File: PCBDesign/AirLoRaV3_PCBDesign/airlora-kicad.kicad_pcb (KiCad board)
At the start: 4 copper layers, 60 x 60 mm, 89 parts, among them IC1 BALFHB-WL-05D3, J1 12V, J2 Conn_Coaxial, J3 DHT, J4 UART1, J5 UART2, J6 I2C, J7 UART2, Q1 S8050, Q2 S8050, Q3 S8050, Q4 S8050, SW1 SW_Push, U1 TPS54202DDC, U2 TPS7A2633DRVR, U3 BGS12WN6E6327, U4 STM32WLE5JCIx, Y1 NX2012SA 32.768KHz

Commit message: Update circuit buck converter and sensor
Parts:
- removed the C17 at (162.3, 88.8)
- removed the C23 at (162.3, 90.3)
- removed the C29 at (158.0, 81.7)
- removed the C31 at (150.1, 96.7)
- removed the C33 at (150.1, 98.2)
- removed the C35 at (151.9, 81.7)
- removed the C36 at (162.3, 87.3)
- removed L5: 1400R 1GHz, Inductor_SMD:L_0603_1608Metric
- removed XTAL1: NT2016SA-32M-END4263A, footprint:NT2016SA-32M-END4263A_NDK
- added C18: 0.47uF, Capacitor_SMD:C_0603_1608Metric, F.Cu at (68.8, 133.7)
- added C27: 4.7uF, Capacitor_SMD:C_0603_1608Metric, F.Cu at (68.8, 136.8)
- added C28: 100nF, Capacitor_SMD:C_0603_1608Metric, F.Cu at (68.8, 135.2)
- added C37: 4.7uf, Capacitor_SMD:C_0805_2012Metric, F.Cu at (228.3, 85.6)
- added C38: 100nf, Capacitor_SMD:C_0603_1608Metric, F.Cu at (234.3, 83.8)
- added C40: 100nf, Capacitor_SMD:C_0603_1608Metric, F.Cu at (245.9, 88.8)
- added C41: 100nf, Capacitor_SMD:C_0603_1608Metric, F.Cu at (239.8, 99.6)
- added C42: 100nf, Capacitor_SMD:C_0603_1608Metric, F.Cu at (228.1, 92.6)
- added C43: 22PF, Capacitor_SMD:C_0603_1608Metric, F.Cu at (225.4, 99.6)
- added C44: 22PF, Capacitor_SMD:C_0603_1608Metric, F.Cu at (214.8, 86.0)
- added C45: 100nF, Capacitor_SMD:C_0603_1608Metric, F.Cu at (214.8, 88.5)
- added C46: 1uF, Capacitor_SMD:C_0805_2012Metric_Pad1.18x1.45mm_HandSolder, F.Cu at (84.5, 69.5)
- added C47: 1uF, Capacitor_SMD:C_0805_2012Metric_Pad1.18x1.45mm_HandSolder, F.Cu at (84.3, 64.0)
- added D4: LED, LED_SMD:LED_0603_1608Metric_Pad1.05x0.95mm_HandSolder, F.Cu at (220.4, 90.6)
- added D5: LED, LED_SMD:LED_0603_1608Metric_Pad1.05x0.95mm_HandSolder, F.Cu at (68.5, 79.4)
- added J3: LED, Connector_JST:JST_XA_B02B-XASK-1-A_1x02_P2.50mm_Vertical, F.Cu at (50.3, 122.6)
- added Q1: S8050, Package_TO_SOT_SMD:SOT-23, F.Cu at (42.7, 124.4)
- added Q6: ZVP2106GTA, Package_TO_SOT_SMD:SOT-223-3_TabPin2, F.Cu at (89.4, 96.6)
- added R13: 1K, Resistor_SMD:R_0603_1608Metric, F.Cu at (39.1, 123.5)
- added R19: 1k, Resistor_SMD:R_0603_1608Metric, F.Cu at (214.8, 91.1)
- added R20: 10k, Resistor_SMD:R_0603_1608Metric, F.Cu at (214.8, 93.6)
- added R21: 10k, Resistor_SMD:R_0603_1608Metric, F.Cu at (214.8, 96.1)
- added R22: 10K, Resistor_SMD:R_0603_1608Metric, F.Cu at (77.0, 66.4)
- added R23: 1.96M, Resistor_SMD:R_0603_1608Metric, F.Cu at (80.0, 66.4)
- added R24: 1.18M, Resistor_SMD:R_0603_1608Metric, F.Cu at (80.1, 68.1)
- added R25: 1k, Resistor_SMD:R_0603_1608Metric, F.Cu at (68.5, 81.0)
- added R26: 10K, Resistor_SMD:R_0603_1608Metric, F.Cu at (82.5, 99.1)
- added R27: 1K, Resistor_SMD:R_0603_1608Metric, F.Cu at (204.3, 106.3)
- added SW2: SW_Slide_DPDT, Button_Switch_THT:SW_E-Switch_EG1271_SPDT, F.Cu at (104.5, 67.9)
- added SW3: SW_Push, Button_Switch_SMD:SW_Push_SPST_NO_Alps_SKRK, F.Cu at (232.7, 104.5)
- added U5: STM32F103C8Tx, Package_QFP:LQFP-48_7x7mm_P0.5mm, F.Cu at (237.1, 91.5)
- added U6: TPS7A2633DRVR, footprint:TPS7A2633DRVR, F.Cu at (84.3, 66.7)
- added X1: NX2016SA-32MHZ, footprint:NX2016SA_NDK, F.Cu at (86.8, 142.5)
- added Y2: 8Mhz, Crystal:Crystal_SMD_3225-4Pin_3.2x2.5mm, F.Cu at (226.0, 103.1)
- C16: renamed from C32; value 5.1pF -> 6.8pF
- C22: renamed from C34; value 10pF -> 6.8pF
- C39: value 100nF -> 100nf
- D1: value 1N4007 -> D_Zener; footprint Diode_SMD:D_SMA -> Diode_SMD:D_SMA_Handsoldering
- IC1: value BALFHB-WL-05D3 -> BALFHB-WL-02D3
- R12: value 220 -> 10K
- U4: value STM32WLE5JCIx -> STM32WLE5CCUx; footprint Package_BGA:ST_UFBGA-73_5x5mm_Layout9x9_P0.5mm -> Package_DFN_QFN:QFN-48-1EP_7x7mm_P0.5mm_EP5.6x5.6mm
- moved H1 225.8 mm to (-46.3, 111.3)
- moved H2 225.8 mm to (-46.3, 61.3)
- moved H3 225.8 mm to (-96.3, 111.3)
- moved H4 225.8 mm to (-96.3, 61.3)
- moved C11 104.8 mm to (269.2, 128.8)
- moved C12 104.8 mm to (266.5, 131.2)
- moved C14 104.8 mm to (266.5, 132.8)
- moved C17 104.8 mm to (262.0, 125.8)
- moved L2 104.8 mm to (274.5, 128.8)
- moved C10 104.8 mm to (271.8, 129.6)
- moved C13 104.8 mm to (267.6, 124.3)
- moved C15 104.8 mm to (267.6, 125.8)
- moved C9 104.8 mm to (277.1, 129.6)
- moved IC1 104.8 mm to (263.0, 128.8)
- moved J2 104.8 mm to (280.7, 128.9)
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- renumbered C21 to C17, C16 to C19, C18 to C20, C19 to C21, C22 to C23, C26 to C24, C28 to C25, C30 to C26, C20 to C29, C24 to C30, C25 to C31, C27 to C32, C37 to C33, C38 to C34, C40 to C35, C41 to C36, J3 to J4, J4 to J5, J5 to J6, J6 to J7, J7 to J8, Q1 to Q2, Q2 to Q3, Q3 to Q4, Q4 to Q5, R13 to R14, R14 to R15, R15 to R16, R16 to R17, R17 to R18
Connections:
- C12 pad 1: Net-(U3-VDD) -> GND
- C12 pad 2: GND -> Net-(U3-VDD)
- C14 pad 1: Net-(U3-VDD) -> GND
- C14 pad 2: GND -> Net-(U3-VDD)
- C16 pad 2: Net-(XTAL1-VCC) -> Net-(U4-OSC_IN)
- C21 pad 1: VDDPA -> VDDRF1V55
- C22 pad 1: Net-(C34-Pad1) -> Net-(U4-OSC_OUT)
- C22 pad 2: XTA -> GND
- C24 pad 1: VDDRF -> +3.3V
- C25 pad 1: VREF+ -> Net-(U4-VDDA)
- C26 pad 1: VREF+ -> Net-(U4-VDDA)
- C29 pad 1: VDDRF -> +3.3V
- C30 pad 1: VDDRF -> +3.3V
- C31 pad 1: VDDRF -> +3.3V
- C32 pad 1: VDDRF -> +3.3V
- C35 pad 1: VDDPA -> VDDRF1V55
- C39 pad 1: VDDPA -> 3.3V
- C8 pad 1: VDDRF -> +3.3V
- D3 pad 2: VDDRF -> +3.3V
- J1 pad 1: Net-(D1-A) -> Net-(J1-Pin_1)
- J4 pad 2: /AirLora V3/MCU/PA11 -> /AirLora V3/MCU Sub/PA1
- J5 pad 3: /AirLora V3/MCU/PA9_TX -> /AirLora V3/MCU Sub/TX3
- J5 pad 4: /AirLora V3/MCU/PA10_RX -> /AirLora V3/MCU Sub/RX3
- J6 pad 3: /AirLora V3/MCU/PA3_RX -> /AirLora V3/MCU Sub/RX2
- J6 pad 4: /AirLora V3/MCU/PA2_TX -> /AirLora V3/MCU Sub/TX2
- J7 pad 3: /AirLora V3/MCU/PB8_SCL -> /AirLora V3/MCU Sub/SDA1
- J7 pad 4: /AirLora V3/MCU/PB9_SDA -> /AirLora V3/MCU Sub/SCL1
- J8 pad 2: VDDRF -> +3.3V
- J8 pad 3: /AirLora V3/MCU/T_SWCLK -> Net-(J8-Pin_3)
- J8 pad 4: /AirLora V3/MCU/T_SWDIO -> Net-(J8-Pin_4)
- L3 pad 1: VDDPA -> VDDRF1V55
- L4 pad 1: VDDRF -> +3.3V
- L4 pad 2: VREF+ -> Net-(U4-VDDA)
- R1 pad 2: /AirLora V3/MCU/PA12 -> /AirLora V3/MCU/PB3
- R10 pad 1: VDDRF -> +3.3V
- R12 pad 1: Net-(XTAL1-OUTPUT) -> GND
- R12 pad 2: Net-(C34-Pad1) -> Net-(U4-PH3)
- R14 pad 1: /AirLora V3/MCU/PA11 -> /AirLora V3/MCU Sub/PA1
- R15 pad 2: /AirLora V3/MCU/PB2 -> /AirLora V3/MCU Sub/PA7
- R16 pad 1: /AirLora V3/MCU/PA6 -> /AirLora V3/MCU Sub/PA6
- R17 pad 1: /AirLora V3/MCU/PA5 -> /AirLora V3/MCU Sub/PA5
- R18 pad 1: /AirLora V3/MCU/PA8 -> /AirLora V3/MCU Sub/PA4
- R6 pad 2: VDDRF -> +3.3V
- R7 pad 1: VDDRF -> +3.3V
- U2 pad 1: VDDRF -> +3.3V
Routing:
- net +5V: track 140.1 -> 24.1 mm, vias 4 -> 0
- net VDDRF: track 79.7 -> 15.0 mm, vias 13 -> 0
- net /AirLora V3/MCU/PA12: track 42.7 -> 0.00 mm, vias 2 -> 0
- net /AirLora V3/MCU/PB9_SDA: track 37.8 -> 0.00 mm, vias 1 -> 0
- net 12V: track 37.1 -> 0.00 mm
- net /AirLora V3/MCU/PA11: track 33.6 -> 0.00 mm, vias 1 -> 0
- net +3.3V: track 0.00 -> 33.1 mm, vias 0 -> 5
- net /AirLora V3/MCU/PA9_TX: track 32.7 -> 0.00 mm, vias 1 -> 0
- net /AirLora V3/MCU/PB8_SCL: track 31.4 -> 0.00 mm, vias 1 -> 0
- net /AirLora V3/MCU/T_SWDIO: track 27.4 -> 0.00 mm, vias 1 -> 0
- net /AirLora V3/MCU/T_SWCLK: track 27.2 -> 1.76 mm
- net /AirLora V3/MCU/PA5: track 25.1 -> 0.00 mm, vias 2 -> 0
- net /AirLora V3/MCU/PB2: track 24.7 -> 0.00 mm, vias 3 -> 0
- net /AirLora V3/MCU/PA10_RX: track 24.2 -> 0.00 mm, vias 1 -> 0
- net /AirLora V3/MCU/PA2_TX: track 23.2 -> 0.00 mm, vias 1 -> 0
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- removed copper zone on In2.Cu, net VDDPA

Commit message: Update schematic
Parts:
- added J10: A_NO2, Connector_JST:JST_XH_B3B-XH-A_1x03_P2.50mm_Vertical, F.Cu at (197.5, 73.2)
- added J11: A_CO, Connector_JST:JST_XH_B3B-XH-A_1x03_P2.50mm_Vertical, F.Cu at (197.1, 85.0)
- added J6: I2C, Connector_Molex:Molex_CLIK-Mate_502585-0470_1x04-1MP_P1.50mm_Horizontal, F.Cu at (167.5, 42.1)
- added Q10: S8050, Package_TO_SOT_SMD:SOT-23, F.Cu at (191.0, 87.2)
- added Q3: S8050, Package_TO_SOT_SMD:SOT-23, F.Cu at (170.5, 107.8)
- added Q6: S8050, Package_TO_SOT_SMD:SOT-23, F.Cu at (170.2, 48.9)
- added Q9: S8050, Package_TO_SOT_SMD:SOT-23, F.Cu at (191.3, 77.3)
- added R20: 1K, Resistor_SMD:R_0603_1608Metric, F.Cu at (171.4, 104.0)
- added R24: 1K, Resistor_SMD:R_0603_1608Metric, F.Cu at (170.3, 53.0)
- added R30: 1K, Resistor_SMD:R_0603_1608Metric, F.Cu at (187.3, 77.3)
- added R31: 1K, Resistor_SMD:R_0603_1608Metric, F.Cu at (186.9, 87.3)
- J3: value LED -> Led; footprint Connector_JST:JST_XA_B02B-XASK-1-A_1x02_P2.50mm_Vertical -> Connector_JST:JST_XH_B3B-XH-A_1x03_P2.50mm_Vertical
- J4: footprint Connector_JST:JST_XH_B3B-XH-A_1x03_P2.50mm_Vertical -> Connector_Molex:Molex_CLIK-Mate_502585-0370_1x03-1MP_P1.50mm_Horizontal
- J5: footprint Connector_JST:JST_XH_B4B-XH-A_1x04_P2.50mm_Vertical -> Connector_Molex:Molex_CLIK-Mate_502585-0470_1x04-1MP_P1.50mm_Horizontal
- J7: renamed from J6; footprint Connector_JST:JST_XH_B4B-XH-A_1x04_P2.50mm_Vertical -> Connector_Molex:Molex_CLIK-Mate_502585-0470_1x04-1MP_P1.50mm_Horizontal
- J8: renamed from J7; footprint Connector_JST:JST_XH_B4B-XH-A_1x04_P2.50mm_Vertical -> Connector_Molex:Molex_CLIK-Mate_502585-0470_1x04-1MP_P1.50mm_Horizontal
- moved H2 248.8 mm to (201.5, 38.8)
- moved H1 247.8 mm to (201.5, 113.7)
- moved H4 229.8 mm to (132.4, 38.8)
- moved H3 228.7 mm to (132.4, 113.7)
- moved Q8 143.0 mm to (145.2, 48.7), turned to 90 degrees
- moved R26 137.9 mm to (145.3, 51.6), turned to 180 degrees
- moved R19 128.7 mm to (166.2, 103.9), turned to -90 degrees
- moved Q2 123.7 mm to (165.3, 107.8), turned to -90 degrees
- moved J3 119.6 mm to (169.6, 114.0), turned to 180 degrees
- moved U5 103.0 mm to (168.8, 90.2)
- moved C21 103.0 mm to (174.0, 81.3)
- moved C24 103.0 mm to (180.6, 95.1)
- moved C32 103.0 mm to (177.2, 82.9)
- moved C34 103.0 mm to (160.4, 91.1)
- moved C18 103.0 mm to (175.8, 95.3)
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- renumbered C8 to C10, C9 to C11, C10 to C12, C11 to C13, C12 to C14, C13 to C15, C14 to C16, C15 to C17, C16 to C18, C17 to C19, C46 to C2, C18 to C20, C19 to C21, C20 to C22, C21 to C23, C22 to C24, C23 to C25, C24 to C26, C25 to C27, C26 to C28, C27 to C29, C2 to C3, C28 to C30, C29 to C31, C30 to C32, C31 to C33, C32 to C34, C33 to C35, C34 to C36, C35 to C37, C36 to C38, C37 to C39, C3 to C4, C38 to C40, C39 to C41, C40 to C42, C41 to C43, C42 to C44, C43 to C45, C44 to C46, C45 to C47, C4 to C5, C5 to C6, C47 to C7, C6 to C8, C7 to C9, D5 to D3, D3 to D4, D4 to D5, J8 to J9, Q6 to Q1, Q1 to Q2, Q2 to Q4, Q3 to Q5, Q4 to Q7, Q5 to Q8, R26 to R1, R25 to R10, R6 to R11, R7 to R12, R8 to R13, R9 to R14, R10 to R15, R11 to R16, R12 to R17, R27 to R18, R13 to R19, R1 to R2, R14 to R21, R15 to R22, R16 to R23, R17 to R25, R18 to R26, R19 to R27, R20 to R28, R21 to R29, R2 to R3, R3 to R4, R22 to R5, R4 to R6, R23 to R7, R24 to R8, R5 to R9, U6 to U2, U2 to U3, U3 to U4, U4 to U5, U5 to U6
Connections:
- J3 pad 2: +5V -> Net-(J3-Pin_2)
- J5 pad 3: /AirLora V3/MCU Sub/TX3 -> /AirLora V3/MCU Sub/RX3
- J5 pad 4: /AirLora V3/MCU Sub/RX3 -> /AirLora V3/MCU Sub/TX3
- J7 pad 3: /AirLora V3/MCU Sub/RX2 -> /AirLora V3/MCU Sub/SCL1
- J7 pad 4: /AirLora V3/MCU Sub/TX2 -> /AirLora V3/MCU Sub/SDA1
- J8 pad 3: /AirLora V3/MCU Sub/SDA1 -> /AirLora V3/MCU Sub/SCL1
- J8 pad 4: /AirLora V3/MCU Sub/SCL1 -> /AirLora V3/MCU Sub/SDA1
- Q2 pad 2: Net-(J3-Pin_1) -> +5V
- Q2 pad 3: GND -> Net-(J3-Pin_2)
- R23 pad 1: /AirLora V3/MCU Sub/PA6 -> /AirLora V3/MCU Sub/PA5
- R25 pad 1: /AirLora V3/MCU Sub/PA5 -> /AirLora V3/MCU Sub/PA4
- R26 pad 1: /AirLora V3/MCU Sub/PA4 -> /AirLora V3/MCU Sub/PA6
- U5 pad 9: unconnected-(U4-PA2-Pad9) -> Net-(U5-PA2)
- U6 pad 18: unconnected-(U5-PB0-Pad18) -> /AirLora V3/MCU Sub/PB0
- U6 pad 19: unconnected-(U5-PB1-Pad19) -> /AirLora V3/MCU Sub/PB1
- U6 pad 38: unconnected-(U5-PA15-Pad38) -> /AirLora V3/MCU Sub/PA15
- U6 pad 39: unconnected-(U5-PB3-Pad39) -> /AirLora V3/MCU Sub/PB3
- U6 pad 40: unconnected-(U5-PB4-Pad40) -> /AirLora V3/MCU Sub/PB4
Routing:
- net Net-(J4-Pin_3): track 16.8 -> 0.00 mm
- net +3.3V: track 33.1 -> 19.3 mm, vias 5 -> 0
- net /AirLora V3/MCU Sub/PA1: track 8.47 -> 0.00 mm
- net Net-(U3-NC): track 6.22 -> 0.00 mm
- net +5V: track 24.1 -> 18.2 mm
- net GND: track 0.27 -> 5.94 mm
- net Net-(U4-VDD): track 5.67 -> 0.00 mm
- net Net-(J7-Pin_2): track 5.11 -> 0.00 mm
- net /AirLora V3/MCU Sub/TX2: track 4.27 -> 0.00 mm
- net Net-(U3-PG): track 2.12 -> 0.00 mm
- net Net-(Q7-B): track 1.69 -> 0.00 mm
- net Net-(Q8-B): track 1.62 -> 0.00 mm
- net /AirLora V3/MCU Sub/RX2: track 1.29 -> 0.00 mm
- net /AirLora V3/MCU Sub/PA4: track 0.95 -> 0.00 mm
- removed copper zone on F.Cu, net VDDRF
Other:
- board size 60 x 60 mm -> 79.1 x 84.9 mm

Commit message: Update PCB
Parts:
- removed the C38 at (192.9, 48.9)
- removed the R21 at (192.9, 50.4)
- J4: value DHT -> SHT; footprint Connector_Molex:Molex_CLIK-Mate_502585-0370_1x03-1MP_P1.50mm_Horizontal -> Connector_JST:JST_XH_B4B-XH-A_1x04_P2.50mm_Vertical
- J9: renamed from J7; value UART2 -> I2C
- SW3: footprint Button_Switch_SMD:SW_Push_SPST_NO_Alps_SKRK -> Button_Switch_SMD:SW_Push_1P1T_NO_Vertical_Wuerth_434133025816
- moved SW1 36.0 mm to (160.5, 94.1)
- moved Q7 33.5 mm to (149.1, 50.8)
- moved J7 33.5 mm to (146.8, 43.7)
- moved R24 33.5 mm to (149.2, 53.7)
- moved C22 32.7 mm to (156.6, 94.0), turned to -90 degrees
- moved R29 24.7 mm to (161.3, 75.9), turned to -90 degrees
- moved SW3 22.6 mm to (157.5, 75.6)
- moved C46 21.1 mm to (153.7, 75.9), turned to 90 degrees
- moved R26 17.5 mm to (175.1, 53.1), turned to 0 degrees
- moved J10 17.4 mm to (159.5, 43.7)
- moved J5 17.4 mm to (184.9, 43.7)
- moved J9 17.4 mm to (172.2, 43.7)
- moved Q10 17.4 mm to (162.5, 50.3)
- moved Q4 17.4 mm to (187.5, 50.5)
- moved Q9 17.4 mm to (175.0, 50.3)
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- renumbered C2 to C1, C1 to C2, C39 to C38, C40 to C39, C41 to C40, C42 to C41, C43 to C42, C44 to C43, C45 to C44, C46 to C45, C47 to C46, C7 to C6, C6 to C7, D3 to D2, D2 to D3, J8 to J10, J9 to J11, J6 to J5, J10 to J6, J5 to J7, J11 to J8, Q8 to Q10, Q6 to Q4, Q4 to Q5, Q9 to Q6, Q5 to Q7, Q10 to Q8, Q7 to Q9, R9 to R10, R24 to R21, R30 to R23, R23 to R24, R31 to R25, R25 to R26, R26 to R27, R27 to R28, R28 to R29, R5 to R3, R29 to R30, R7 to R4, R8 to R5, R3 to R6, R4 to R7, R6 to R8, R10 to R9, U2 to U1, U1 to U2
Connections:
- net 12V renamed +12V
- net 3.3V renamed +3.3V_HP
- J4 pad 2: /AirLora V3/MCU Sub/PA1 -> Net-(J4-Pin_2)
- J4 pad 3: Net-(J4-Pin_3) -> /AirLora V3/MCU Sub/SCL1
- Q5 pad 3: Net-(J4-Pin_3) -> Net-(J4-Pin_2)
- R19 pad 1: Net-(U5-PA1) -> Net-(U5-PA5)
- R2 pad 2: /AirLora V3/MCU/PB3 -> /AirLora V3/MCU/PA3
- R20 pad 1: Net-(U5-PA2) -> Net-(U5-PA6)
- R23 pad 1: /AirLora V3/MCU Sub/PB4 -> /AirLora V3/MCU Sub/PA6
- R25 pad 1: /AirLora V3/MCU Sub/PB3 -> /AirLora V3/MCU Sub/PA4
- R26 pad 1: /AirLora V3/MCU Sub/PA4 -> /AirLora V3/MCU Sub/PB3
- R27 pad 1: /AirLora V3/MCU Sub/PA6 -> /AirLora V3/MCU Sub/PB4
- U5 pad 1: /AirLora V3/MCU/PB3 -> unconnected-(U5-PB3-Pad1)
- U5 pad 10: unconnected-(U5-PA3-Pad10) -> /AirLora V3/MCU/PA3
- U5 pad 13: unconnected-(U5-PA5-Pad13) -> Net-(U5-PA5)
- U5 pad 14: unconnected-(U5-PA6-Pad14) -> Net-(U5-PA6)
- U5 pad 34: unconnected-(U5-PA11-Pad34) -> /AirLora V3/MCU Sub/SCL2
- U5 pad 35: unconnected-(U5-PA12-Pad35) -> /AirLora V3/MCU Sub/SDA2
- U5 pad 4: /AirLora V3/MCU Sub/SCL2 -> unconnected-(U5-PB6-Pad4)
- U5 pad 5: /AirLora V3/MCU Sub/SDA2 -> unconnected-(U5-PB7-Pad5)
- U5 pad 8: Net-(U5-PA1) -> unconnected-(U5-PA1-Pad8)
- U5 pad 9: Net-(U5-PA2) -> unconnected-(U5-PA2-Pad9)
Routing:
- net +5V: track 18.2 -> 260.8 mm, vias 0 -> 8
- net +3.3V: track 19.3 -> 160.9 mm, vias 0 -> 8
- net +3.3V_HP: track 0.00 -> 112.8 mm, vias 0 -> 3
- net /AirLora V3/MCU Sub/SDA1: track 0.00 -> 79.1 mm, vias 0 -> 2
- net /AirLora V3/MCU Sub/SCL1: track 0.00 -> 64.7 mm, vias 0 -> 2
- net +12V: track 0.00 -> 48.9 mm, vias 0 -> 2
- net /AirLora V3/MCU Sub/TX3: track 0.00 -> 41.3 mm, vias 0 -> 2
- net /AirLora V3/MCU Sub/RX3: track 0.00 -> 41.3 mm, vias 0 -> 2
- net /AirLora V3/MCU Sub/PB1: track 0.00 -> 41.2 mm
- net /AirLora V3/MCU Sub/PA7: track 0.00 -> 37.3 mm, vias 0 -> 2
- net /AirLora V3/MCU Sub/SDA2: track 0.00 -> 36.4 mm, vias 0 -> 2
- net /AirLora V3/MCU Sub/SCL2: track 0.00 -> 34.0 mm, vias 0 -> 2
- net /AirLora V3/MCU Sub/PA4: track 0.00 -> 32.2 mm, vias 0 -> 2
- net /AirLora V3/MCU Sub/PB0: track 0.00 -> 32.2 mm, vias 0 -> 1
- net /AirLora V3/MCU Sub/PA8: track 0.00 -> 31.4 mm, vias 0 -> 2
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- added copper zone on F.Cu, net +3.3V
- added copper zone on F.Cu, net +3.3V_HP
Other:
- board size 79.1 x 84.9 mm -> 77 x 77 mm

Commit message: Update PCB
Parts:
- moved R2 0.41 mm to (138.6, 86.4)
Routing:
- net /AirLora V3/MCU Sub/PA8: track 31.4 -> 35.7 mm
- net Net-(J4-Pin_2): track 17.8 -> 14.3 mm
- net /AirLora V3/MCU Sub/PB1: track 41.2 -> 43.7 mm
- net Net-(U5-PA5): track 11.4 -> 12.8 mm
- net Net-(U5-PC13): track 25.9 -> 25.1 mm
- net /AirLora V3/MCU Sub/SDA1: track 79.1 -> 79.9 mm
- net /AirLora V3/MCU/T_SWCLK: track 25.0 -> 24.3 mm
- net Net-(U5-NRST): track 15.7 -> 16.4 mm
- net +5V: track 260.8 -> 261.3 mm
- net +3.3V_HP: track 112.8 -> 113.3 mm

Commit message: Update package and placement components
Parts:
- added C47: 0.47uF, Capacitor_SMD:C_0402_1005Metric_Pad0.74x0.62mm_HandSolder, F.Cu at (185.4, 91.5)
- added C48: 470nF, Capacitor_SMD:C_0402_1005Metric_Pad0.74x0.62mm_HandSolder, F.Cu at (185.4, 92.5)
- added C49: 100pF, Capacitor_SMD:C_0402_1005Metric_Pad0.74x0.62mm_HandSolder, F.Cu at (174.4, 106.5)
- added C50: 100pF, Capacitor_SMD:C_0402_1005Metric_Pad0.74x0.62mm_HandSolder, F.Cu at (178.3, 93.2)
- added L5: NC, Inductor_SMD:L_0402_1005Metric_Pad0.77x0.64mm_HandSolder, F.Cu at (185.4, 93.4)
- C11, C12, C13, C14, C15, C16, C17, C18, C19, C20, C21, C22, C23, C24, C25, C26, C27, C28, C29, C30, C31, C32, C33, C34, C36, C37, C39, C4, C40, C41, C42, C43, C44, C45, C46, C5: footprint Capacitor_SMD:C_0603_1608Metric -> Capacitor_SMD:C_0402_1005Metric_Pad0.74x0.62mm_HandSolder
- C35: value 33pF -> 100pF; footprint Capacitor_SMD:C_0603_1608Metric -> Capacitor_SMD:C_0402_1005Metric_Pad0.74x0.62mm_HandSolder
- C38: footprint Capacitor_SMD:C_0805_2012Metric -> Capacitor_SMD:C_0402_1005Metric_Pad0.74x0.62mm_HandSolder
- L2, L4: footprint Inductor_SMD:L_0603_1608Metric -> Inductor_SMD:L_0402_1005Metric_Pad0.77x0.64mm_HandSolder
- L3: footprint Capacitor_SMD:C_0603_1608Metric_Pad1.08x0.95mm_HandSolder -> Inductor_SMD:L_0402_1005Metric_Pad0.77x0.64mm_HandSolder
- R1, R10, R11, R12, R13, R14, R15, R16, R17, R18, R19, R2, R20, R21, R22, R23, R24, R25, R26, R27, R28, R29, R3, R30, R4, R5, R6, R7, R8, R9: footprint Resistor_SMD:R_0603_1608Metric -> Resistor_SMD:R_0402_1005Metric_Pad0.72x0.64mm_HandSolder
- moved L3 29.6 mm to (172.3, 106.5), turned to 90 degrees
- moved C32 27.7 mm to (179.1, 106.3), turned to -90 degrees
- moved C30 25.9 mm to (173.4, 106.5), turned to -90 degrees
- moved C9 25.0 mm to (153.5, 88.3)
- moved R11 25.0 mm to (149.5, 86.6)
- moved R13 25.0 mm to (149.5, 83.6)
- moved C10 25.0 mm to (153.5, 83.5)
- moved R12 25.0 mm to (149.5, 85.1)
- moved U3 25.0 mm to (153.3, 85.9)
- moved C34 24.8 mm to (178.1, 106.3), turned to -90 degrees
- moved C26 23.2 mm to (168.6, 101.6), turned to 180 degrees
- moved C23 23.2 mm to (168.6, 102.6)
- moved C20 22.7 mm to (168.6, 103.6)
- moved J11 22.5 mm to (196.2, 82.4)
- moved C27 22.0 mm to (168.6, 100.6), turned to 180 degrees
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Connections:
- net Net-(U5-RFO_HP) renamed RFO_IN
- U5 pad 24: unconnected-(U5-VR_PA-Pad24) -> Net-(U5-VR_PA)
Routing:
- net +3.3V: track 161.0 -> 13.8 mm, vias 8 -> 0
- net +5V: track 261.3 -> 134.0 mm, vias 8 -> 4
- net /AirLora V3/MCU Sub/PB1: track 43.7 -> 0.00 mm
- net +3.3V_HP: track 113.3 -> 70.0 mm, vias 3 -> 1
- net +12V: track 48.9 -> 5.96 mm, vias 2 -> 0
- net VDDRF1V55: track 34.0 -> 0.00 mm, vias 2 -> 0
- net /AirLora V3/MCU Sub/PA7: track 37.3 -> 3.47 mm, vias 2 -> 1
- net /AirLora V3/MCU Sub/PB0: track 32.2 -> 0.00 mm, vias 1 -> 0
- net VDDRF: track 32.1 -> 0.00 mm, vias 2 -> 0
- net /AirLora V3/MCU Sub/SCL2: track 34.0 -> 4.09 mm, vias 2 -> 1
- net /AirLora V3/MCU Sub/PA4: track 32.2 -> 3.77 mm, vias 2 -> 1
- net /AirLora V3/MCU Sub/PA6: track 30.8 -> 2.58 mm, vias 2 -> 1
- net /AirLora V3/MCU/PA3: track 27.6 -> 0.00 mm
- net Net-(U5-PC13): track 25.1 -> 0.00 mm, vias 2 -> 0
- net /AirLora V3/MCU/T_SWDIO: track 24.8 -> 0.00 mm, vias 1 -> 0
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- added copper zone on In2.Cu, net SW

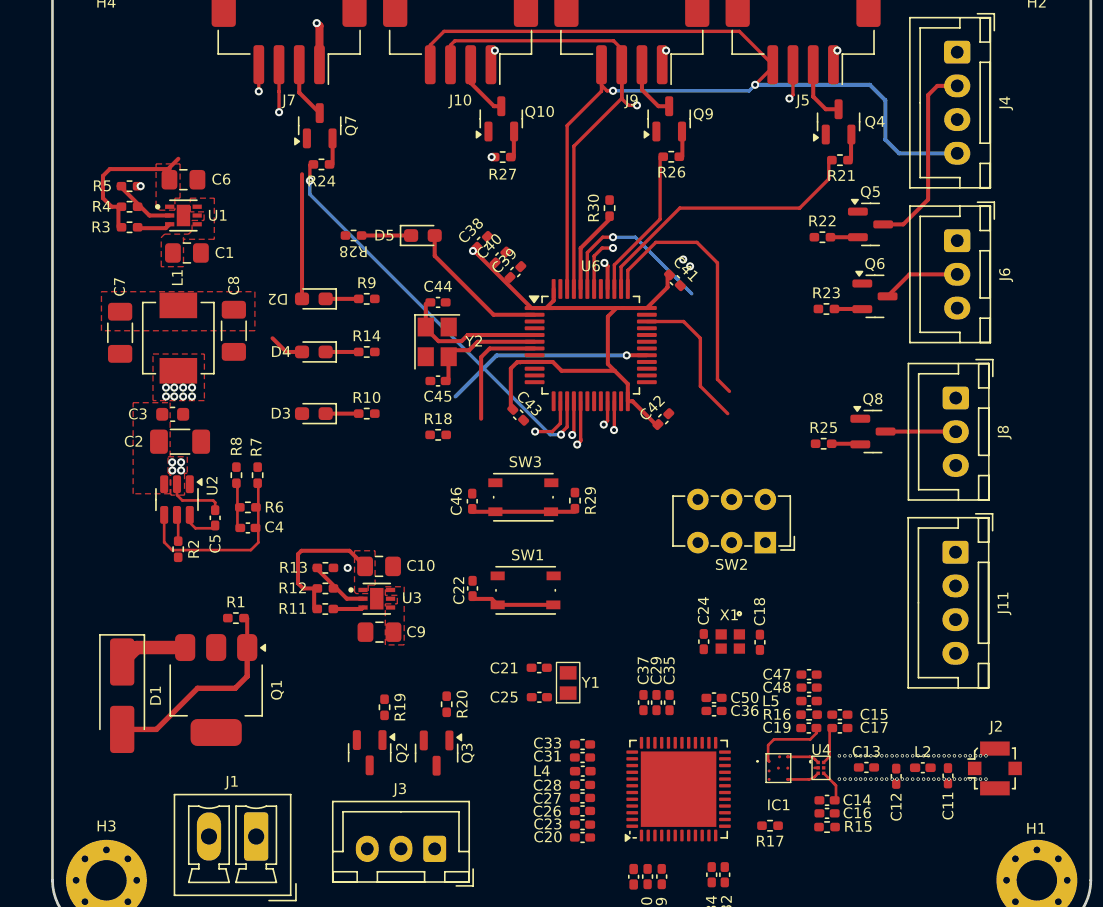
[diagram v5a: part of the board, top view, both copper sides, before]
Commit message: Update Placement component
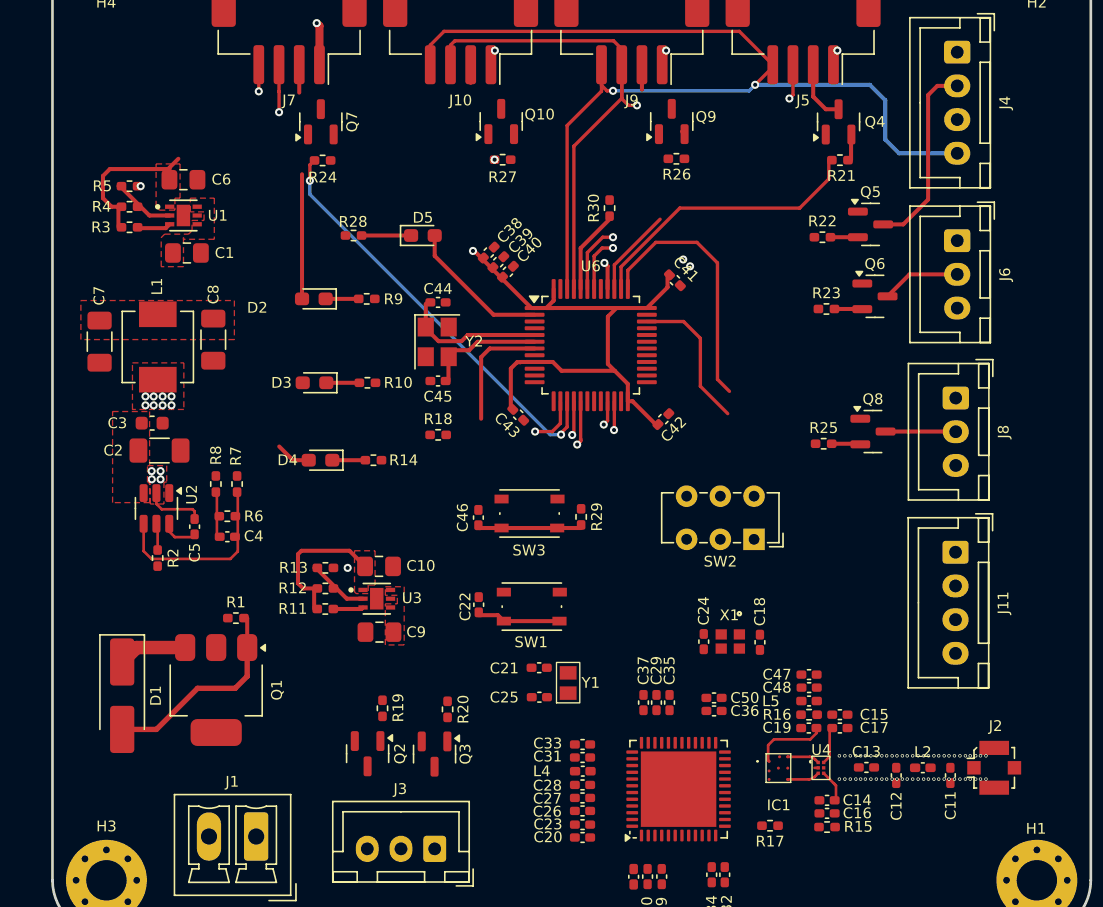
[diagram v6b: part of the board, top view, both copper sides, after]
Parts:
- moved D4 8.04 mm to (149.1, 75.6)
- moved R14 8.04 mm to (153.0, 75.6)
- moved D3 2.29 mm to (148.7, 69.8)
- moved R10 2.29 mm to (152.6, 69.8)
- moved C4 1.66 mm to (142.2, 81.3)
- moved C7 1.66 mm to (132.7, 66.8)
- moved R6 1.66 mm to (142.2, 79.7)
- moved U2 1.66 mm to (137.0, 79.2)
- moved C2 1.66 mm to (137.2, 74.9)
- moved C3 1.66 mm to (136.6, 72.8)
- moved C5 1.66 mm to (139.8, 80.5)
- moved C8 1.66 mm to (141.2, 66.7)
- moved L1 1.66 mm to (137.1, 67.2)
- moved R2 1.66 mm to (137.0, 82.8)
- moved R7 1.66 mm to (142.9, 77.4)
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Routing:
- net /AirLora V3/MCU Sub/PA8: track 15.5 -> 0.00 mm, vias 1 -> 0
- net /AirLora V3/MCU Sub/SDA2: track 12.7 -> 5.07 mm
- net /AirLora V3/MCU Sub/PB3: track 11.2 -> 6.58 mm
- net Net-(J10-Pin_2): track 4.33 -> 1.35 mm
- net Net-(J9-Pin_2): track 4.38 -> 1.86 mm
- net Net-(J7-Pin_2): track 4.22 -> 2.07 mm
- net Net-(Q7-B): track 1.93 -> 0.01 mm
- net Net-(Q10-B): track 1.90 -> 0.02 mm
- net Net-(Q9-B): track 1.88 -> 0.04 mm
